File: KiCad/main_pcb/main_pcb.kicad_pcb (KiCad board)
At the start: 0 parts

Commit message: feat(KiCad): Continues work
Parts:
- added C1: 100nF, Capacitor_SMD:C_0201_0603Metric_Pad0.64x0.40mm_HandSolder, F.Cu at (194.6, 71.0)
- added C2: 100nF, Capacitor_SMD:C_0201_0603Metric_Pad0.64x0.40mm_HandSolder, F.Cu at (179.9, 77.0)
- added C20: 10uF, Capacitor_SMD:C_0201_0603Metric_Pad0.64x0.40mm_HandSolder, F.Cu at (183.1, 89.0)
- added C21: 100nF, Capacitor_SMD:C_0201_0603Metric_Pad0.64x0.40mm_HandSolder, F.Cu at (192.6, 85.5)
- added C22: 100nF, Capacitor_SMD:C_0201_0603Metric_Pad0.64x0.40mm_HandSolder, F.Cu at (168.0, 94.0)
- added C23: 100nF, Capacitor_SMD:C_0201_0603Metric_Pad0.64x0.40mm_HandSolder, F.Cu at (185.9, 92.5)
- added C24: 100nF, Capacitor_SMD:C_0201_0603Metric_Pad0.64x0.40mm_HandSolder, F.Cu at (175.1, 95.0)
- added C25: 100nF, Capacitor_SMD:C_0201_0603Metric_Pad0.64x0.40mm_HandSolder, F.Cu at (188.6, 100.0)
- added C26: 100nF, Capacitor_SMD:C_0201_0603Metric_Pad0.64x0.40mm_HandSolder, F.Cu at (179.1, 98.0)
- added C27: 100nF, Capacitor_SMD:C_0201_0603Metric_Pad0.64x0.40mm_HandSolder, F.Cu at (183.1, 103.0)
- added C28: 100nF, Capacitor_SMD:C_0201_0603Metric_Pad0.64x0.40mm_HandSolder, F.Cu at (172.6, 89.0)
- added C29: 100nF, Capacitor_SMD:C_0201_0603Metric_Pad0.64x0.40mm_HandSolder, F.Cu at (190.6, 96.0)
- added C3: 27pF, Capacitor_SMD:C_0201_0603Metric_Pad0.64x0.40mm_HandSolder, F.Cu at (184.0, 74.5)
- added C30: 100nF, Capacitor_SMD:C_0201_0603Metric_Pad0.64x0.40mm_HandSolder, F.Cu at (166.5, 99.0)
- added C31: 100nF, Capacitor_SMD:C_0201_0603Metric_Pad0.64x0.40mm_HandSolder, F.Cu at (177.1, 104.0)
- added C32: 100nF, Capacitor_SMD:C_0201_0603Metric_Pad0.64x0.40mm_HandSolder, F.Cu at (196.6, 99.0)
- added C33: 100nF, Capacitor_SMD:C_0201_0603Metric_Pad0.64x0.40mm_HandSolder, F.Cu at (192.5, 106.5)
- added C4: 27pF, Capacitor_SMD:C_0201_0603Metric_Pad0.64x0.40mm_HandSolder, F.Cu at (186.9, 78.0)
- added C5: 100nF, Capacitor_SMD:C_0201_0603Metric_Pad0.64x0.40mm_HandSolder, F.Cu at (187.1, 86.0)
- added C6: 100nF, Capacitor_SMD:C_0201_0603Metric_Pad0.64x0.40mm_HandSolder, F.Cu at (176.6, 67.5)
- added C7: 100nF, Capacitor_SMD:C_0201_0603Metric_Pad0.64x0.40mm_HandSolder, F.Cu at (181.1, 81.8)
- added C8: 0.1uF, Capacitor_SMD:C_0201_0603Metric_Pad0.64x0.40mm_HandSolder, F.Cu at (178.4, 88.0)
- added C9: 0.1uF, Capacitor_SMD:C_0201_0603Metric_Pad0.64x0.40mm_HandSolder, F.Cu at (166.6, 89.0)
- added D1: ~, LED_SMD:LED_0603_1608Metric_Pad1.05x0.95mm_HandSolder, F.Cu at (125.9, 79.2)
- added D2: ~, LED_SMD:LED_0603_1608Metric_Pad1.05x0.95mm_HandSolder, F.Cu at (125.9, 81.0)
- added D3: ~, LED_SMD:LED_0603_1608Metric_Pad1.05x0.95mm_HandSolder, F.Cu at (125.9, 82.8)
- added D4: ~, LED_SMD:LED_0603_1608Metric_Pad1.05x0.95mm_HandSolder, F.Cu at (125.9, 77.5)
- added R1: 10kΩ, Resistor_SMD:R_0201_0603Metric_Pad0.64x0.40mm_HandSolder, F.Cu at (190.1, 89.5)
- added R10: 10kΩ, Resistor_SMD:R_0201_0603Metric_Pad0.64x0.40mm_HandSolder, F.Cu at (170.6, 102.5)
- added R11: 10kΩ, Resistor_SMD:R_0201_0603Metric_Pad0.64x0.40mm_HandSolder, F.Cu at (199.1, 93.5)
- added R2: 5.1kΩ, Resistor_SMD:R_0201_0603Metric_Pad0.64x0.40mm_HandSolder, F.Cu at (180.0, 92.0)
- added R3: 5.1kΩ, Resistor_SMD:R_0201_0603Metric_Pad0.64x0.40mm_HandSolder, F.Cu at (175.1, 85.0)
- added R4: 10kΩ, Resistor_SMD:R_0201_0603Metric_Pad0.64x0.40mm_HandSolder, F.Cu at (133.4, 79.0)
- added R5: 10kΩ, Resistor_SMD:R_0201_0603Metric_Pad0.64x0.40mm_HandSolder, F.Cu at (133.4, 81.2)
- added R6: 10kΩ, Resistor_SMD:R_0201_0603Metric_Pad0.64x0.40mm_HandSolder, F.Cu at (133.4, 83.8)
- added R7: 10kΩ, Resistor_SMD:R_0201_0603Metric_Pad0.64x0.40mm_HandSolder, F.Cu at (133.4, 76.8)
- added R8: 10kΩ, Resistor_SMD:R_0201_0603Metric_Pad0.64x0.40mm_HandSolder, F.Cu at (171.1, 107.0)
- added R9: 10kΩ, Resistor_SMD:R_0201_0603Metric_Pad0.64x0.40mm_HandSolder, F.Cu at (193.6, 92.0)
- added U1: ~, Package_QFP:TQFP-100_14x14mm_P0.5mm, F.Cu at (155.3, 76.5)
- added U8: CH340C, lilys_pad:CH340C, F.Cu at (146.9, 88.4)
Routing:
- net /SS: track 0.00 -> 15.0 mm
- net /MISO: track 0.00 -> 15.0 mm
- net /SCK: track 0.00 -> 14.2 mm
- net /MOSI: track 0.00 -> 14.1 mm
- net Net-(D3-Pad1): track 0.00 -> 6.69 mm
- net Net-(D4-Pad1): track 0.00 -> 6.56 mm
- net Net-(D2-Pad1): track 0.00 -> 6.38 mm
- net Net-(D1-Pad1): track 0.00 -> 6.38 mm
- net GND: track 0.00 -> 5.32 mm, vias 0 -> 5
- added copper zone on B.Cu, net GND
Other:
- copper layers 0 -> 2

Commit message: feat(KiCad): Continues work
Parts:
- added J3: ~, Connector_JST:JST_XH_B10B-XH-A_1x10_P2.50mm_Vertical, F.Cu at (110.5, 57.9)
- added J4: 2X4 Header, Connector_JST:JST_XH_B8B-XH-A_1x08_P2.50mm_Vertical, F.Cu at (110.5, 65.7)
- added J5: 1x1 Header, Connector_JST:JST_XH_B1B-XH-AM_1x01_P2.50mm_Vertical, F.Cu at (110.5, 81.2)
- added J6: 1x1 Header, Connector_JST:JST_XH_B1B-XH-AM_1x01_P2.50mm_Vertical, F.Cu at (125.5, 95.0)
- added S2: ~, Button_Switch_THT:SW_PUSH-12mm, F.Cu at (138.5, 102.5)
- added Y1: ~, Crystal:Crystal_SMD_ECS_CSM3X-2Pin_7.6x4.1mm, F.Cu at (158.5, 94.2)
- moved R1 37.8 mm to (154.5, 102.4), turned to -90 degrees
- moved C4 37.8 mm to (152.8, 94.2)
- moved C3 28.0 mm to (164.2, 94.2), turned to 180 degrees
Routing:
- net uC_Reset: track 0.00 -> 22.1 mm
- net Net-(U1-XTAL1): track 0.00 -> 16.0 mm
- net Net-(U1-XTAL2): track 0.00 -> 10.3 mm
- net Net-(C4-Pad2): track 0.00 -> 2.53 mm
- net Net-(C3-Pad2): track 0.00 -> 2.51 mm

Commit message: feat(KiCad): Continues work
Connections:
- net Net-(U1-XTAL1) renamed /Y-
- net Net-(U1-XTAL2) renamed /Y+
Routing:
- net /Y-: track 16.0 -> 0.00 mm
- net /Y+: track 10.3 -> 0.00 mm
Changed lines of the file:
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@@
 	(net 44 "unconnected-(U1-PG5-Pad1)")
 	(net 45 "unconnected-(U1-PE0-Pad2)")
-	(net 46 "Net-(U1-XTAL2)")
+	(net 46 "/Y-")
 	(net 47 "/C4")
 	(net 48 "unconnected-(U1-PE3-Pad5)")
@@
 	(net 85 "/C5")
 	(net 86 "/C2")
-	(net 87 "Net-(U1-XTAL1)")
+	(net 87 "/Y+")
 	(net 88 "unconnected-(U1-PD5-Pad48)")
 	(net 89 "unconnected-(U1-PD4-Pad47)")
@@
 			(layers "F.Cu" "F.Mask" "F.Paste")
 			(roundrect_rratio 0.25)
-			(net 46 "Net-(U1-XTAL2)")
+			(net 87 "/Y+")
 			(pinfunction "XTAL2")
 			(pintype "output")
@@
 			(layers "F.Cu" "F.Mask" "F.Paste")
 			(roundrect_rratio 0.25)
-			(net 87 "Net-(U1-XTAL1)")
+			(net 46 "/Y-")
 			(pinfunction "XTAL1")
 			(pintype "input")
@@
 			(layers "F.Cu" "F.Mask")
 			(roundrect_rratio 0.25)
-			(net 87 "Net-(U1-XTAL1)")
+			(net 46 "/Y-")
 			(pintype "passive")
 		)
@@
 			(layers "F.Cu" "F.Mask")
 			(roundrect_rratio 0.25)
-			(net 46 "Net-(U1-XTAL2)")
+			(net 87 "/Y+")
 			(pintype "passive")
 		)
@@
 	)
 	(segment
-		(start 152.8375 93.751544)
-		(end 152.41 94.179044)
-		(width 0.2)
-		(layer "F.Cu")
-		(net 46)
-	)
-	(segment
-		(start 152.41 94.179044)
-		(end 152.41 94.25)
-		(width 0.2)
-		(layer "F.Cu")
-		(net 46)
-	)
-	(segment
-		(start 152.8375 84.1625)
-		(end 152.8375 93.751544)
-		(width 0.2)
-		(layer "F.Cu")
-		(net 46)
-	)
-	(segment
 		(start 134.59 80.5)
 		(end 147.675 80.5)
@@
 	)
 	(segment
-		(start 163.874999 93.35)
-		(end 164.575 94.050001)
-		(width 0.2)
-		(layer "F.Cu")
-		(net 87)
-	)
-	(segment
-		(start 164.575 94.050001)
-		(end 164.575 94.25)
-		(width 0.2)
-		(layer "F.Cu")
-		(net 87)
-	)
-	(segment
-		(start 161.75509 93.35)
-		(end 163.874999 93.35)
-		(width 0.2)
-		(layer "F.Cu")
-		(net 87)
-	)
-	(segment
-		(start 153.3375 84.93241)
-		(end 161.75509 93.35)
-		(width 0.2)
-		(layer "F.Cu")
-		(net 87)
-	)
-	(segment
-		(start 153.3375 84.1625)
-		(end 153.3375 84.93241)
-		(width 0.2)
-		(layer "F.Cu")
-		(net 87)
-	)
-	(segment

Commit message: feat(KiCad): Continues work
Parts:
- removed C21, C22, C23, C24, C25, C26, C27, C28, C29, C30, C31, C32, C33: 100nF, Capacitor_SMD:C_0201_0603Metric_Pad0.64x0.40mm_HandSolder
- removed S2: ~, Button_Switch_THT:SW_PUSH-12mm
- removed U8: CH340C, lilys_pad:CH340C
- added C10: 0.1uF, Capacitor_SMD:C_0201_0603Metric_Pad0.64x0.40mm_HandSolder, F.Cu at (165.5, 64.4)
- added C11: 0.1uF, Capacitor_SMD:C_0201_0603Metric_Pad0.64x0.40mm_HandSolder, F.Cu at (167.5, 64.4)
- added C12: 100nF, Capacitor_SMD:C_0201_0603Metric_Pad0.64x0.40mm_HandSolder, F.Cu at (143.4, 96.5)
- added C13: 100nF, Capacitor_SMD:C_0201_0603Metric_Pad0.64x0.40mm_HandSolder, F.Cu at (143.4, 98.2)
- added C14: 100nF, Capacitor_SMD:C_0201_0603Metric_Pad0.64x0.40mm_HandSolder, F.Cu at (143.4, 100.0)
- added C15: 100nF, Capacitor_SMD:C_0201_0603Metric_Pad0.64x0.40mm_HandSolder, F.Cu at (143.4, 101.8)
- added C16: 100nF, Capacitor_SMD:C_0201_0603Metric_Pad0.64x0.40mm_HandSolder, F.Cu at (143.4, 103.5)
- added C17: 100nF, Capacitor_SMD:C_0201_0603Metric_Pad0.64x0.40mm_HandSolder, F.Cu at (146.3, 96.5)
- added C18: 100nF, Capacitor_SMD:C_0201_0603Metric_Pad0.64x0.40mm_HandSolder, F.Cu at (146.3, 98.2)
- added C19: 100nF, Capacitor_SMD:C_0201_0603Metric_Pad0.64x0.40mm_HandSolder, F.Cu at (146.3, 100.0)
- added J2: ~, Connector_JST:JST_XH_B10B-XH-A_1x10_P2.50mm_Vertical, F.Cu at (108.5, 83.0)
- added S1: ~, Button_Switch_THT:SW_PUSH-12mm, F.Cu at (125.4, 92.7)
- added U2: CH340C, Lilibrary:SOIC127P600X180-16N, F.Cu at (167.0, 74.5)
- added U3: JSMSEMI AMS1117-3.3V, Lilibrary:SOT229P700X180-4N, F.Cu at (167.2, 57.2)
- added U4: TI TXB0104DR, Lilibrary:SOIC127P600X175-14N, F.Cu at (166.1, 141.7)
- added U6: TI TXB0104DR, Lilibrary:SOIC127P600X175-14N, F.Cu at (175.0, 141.7)
- added U9: TI TXB0104DR, Lilibrary:SOIC127P600X175-14N, F.Cu at (184.0, 141.7)
- C2: value 100nF -> 27pF
- C20: value 10uF -> 100nF
- C4: value 27pF -> 100nF
- C8: value 0.1uF -> 100nF
- C9: value 0.1uF -> 10uF
- J3: value ~ -> 1x6 Header; footprint Connector_JST:JST_XH_B10B-XH-A_1x10_P2.50mm_Vertical -> Lilibrary:1x6 Header
- J4: value 2X4 Header -> 1x1 Header; footprint Connector_JST:JST_XH_B8B-XH-A_1x08_P2.50mm_Vertical -> Lilibrary:1x1 Header
- J5: footprint Connector_JST:JST_XH_B1B-XH-AM_1x01_P2.50mm_Vertical -> Lilibrary:1x1 Header
- J6: value 1x1 Header -> USB-C; footprint Connector_JST:JST_XH_B1B-XH-AM_1x01_P2.50mm_Vertical -> Lilibrary:HRO_TYPE-C-31-M-12
- R2, R3: value 5.1kΩ -> 330Ω
- R4, R5: value 10kΩ -> 330Ω
- R6, R7: value 10kΩ -> 5.1kΩ
- moved J3 103.9 mm to (132.5, 159.5), turned to -90 degrees
- moved C1 75.7 mm to (129.3, 109.5), turned to 0 degrees
- moved U1 70.8 mm to (132.5, 143.5), turned to 90 degrees
- moved C5 65.3 mm to (129.3, 116.5)
- moved J6 61.3 mm to (180.5, 122.0)
- moved C2 61.1 mm to (129.3, 111.2)
- moved R2 51.0 mm to (132.1, 109.5)
- moved R11 50.4 mm to (149.1, 100.0)
- moved R3 50.3 mm to (132.1, 111.2)
- moved J5 44.8 mm to (155.3, 83.0)
- moved R9 44.7 mm to (149.1, 96.5)
- moved J4 41.6 mm to (148.3, 83.0)
- moved D4 41.4 mm to (135.8, 117.7), turned to 0 degrees
- moved C3 39.6 mm to (129.3, 113.0), turned to 0 degrees
- moved C20 39.0 mm to (146.3, 101.8)
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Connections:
- C1 pad 1: GND -> VCC
- C1 pad 2: Net-(U8-V3) -> VCC
- C2 pad 1: Net-(U8-DTR#) -> /Y-
- C2 pad 2: uC_Reset -> Net-(C2-Pad2)
- C20 pad 1: VCC -> GND
- C20 pad 2: GND -> 3V3
- C3 pad 1: /Y- -> /Y+
- C4 pad 1: /Y+ -> Net-(U1-AREF)
- C4 pad 2: Net-(C4-Pad2) -> GND
- C5 pad 1: VCC -> GND
- C5 pad 2: VCC -> GND
- C6 pad 1: GND -> VCC
- C7 pad 2: VCC -> uC_Reset
- C8 pad 1: VCC -> GND
- C8 pad 2: GND -> Net-(U2-V3)
- J3 pad 1: /TCK -> /SS
- J3 pad 2: GND -> /MISO
- J3 pad 3: /TDO -> /MOSI
- J3 pad 4: VCC -> /SCK
- J3 pad 5: /TMS -> VCC
- J3 pad 6: uC_Reset -> GND
- J4 pad 1: /SCK -> VCC
- R2 pad 1: Net-(J2-CC1) -> Net-(D1-Pad1)
- R2 pad 2: GND -> /SS
- R3 pad 1: Net-(J2-CC2) -> Net-(D2-Pad1)
- R3 pad 2: GND -> /MISO
- R4 pad 1: Net-(D1-Pad1) -> Net-(D3-Pad1)
- R4 pad 2: /SCK -> /MOSI
- R5 pad 1: Net-(D2-Pad1) -> Net-(D4-Pad1)
- R5 pad 2: /MOSI -> /SCK
- R6 pad 1: Net-(D3-Pad1) -> Net-(J6-CC1)
- R6 pad 2: /MISO -> GND
- R7 pad 1: Net-(D4-Pad1) -> Net-(J6-CC2)
- R7 pad 2: /SS -> GND
- U1 pad 12: unconnected-(U1-PH0-Pad12) -> /screens/LED/BL
- Y1 pad 1: Net-(C3-Pad2) -> Net-(C2-Pad2)
- Y1 pad 2: Net-(C4-Pad2) -> Net-(C3-Pad2)
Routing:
- net uC_Reset: track 22.1 -> 0.00 mm
- net /SS: track 15.0 -> 0.00 mm
- net /MISO: track 15.0 -> 0.00 mm
- net /SCK: track 14.2 -> 0.00 mm
- net /MOSI: track 14.1 -> 0.00 mm
- net VCC: track 0.00 -> 11.4 mm
- net Net-(D3-Pad1): track 6.69 -> 0.00 mm
- net Net-(D4-Pad1): track 6.56 -> 0.00 mm
- net Net-(D2-Pad1): track 6.38 -> 0.00 mm
- net Net-(D1-Pad1): track 6.38 -> 0.00 mm
- net GND: track 5.32 -> 0.00 mm, vias 5 -> 0
- net Net-(C4-Pad2): track 2.53 -> 0.00 mm
- net Net-(C3-Pad2): track 2.51 -> 0.00 mm
- removed copper zone on B.Cu, net GND

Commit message: Adds Main PCB layout (#38)
* feat(PCB): PCB first draft
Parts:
- removed C5: 100nF, Capacitor_SMD:C_0201_0603Metric_Pad0.64x0.40mm_HandSolder
- removed J2: ~, Connector_JST:JST_XH_B10B-XH-A_1x10_P2.50mm_Vertical
- removed R10, R11, R8, R9: 10kΩ, Resistor_SMD:R_0201_0603Metric_Pad0.64x0.40mm_HandSolder
- added J1: 1x21 Header, Lilibrary:1x21 Header, F.Cu at (122.0, 173.0)
- added J7: 1X7 Header, Lilibrary:1x7 Header, F.Cu at (140.4, 64.7)
- added J8: 1X7 Header, Lilibrary:1x7 Header, F.Cu at (121.5, 64.7)
- added J9: 1x13 Header, Lilibrary:1x13 Header, F.Cu at (94.8, 64.8)
- C1, C10, C11, C12, C13, C14, C15, C16, C17, C18, C19, C2, C20, C3, C4, C6, C7, C8, C9: footprint Capacitor_SMD:C_0201_0603Metric_Pad0.64x0.40mm_HandSolder -> Capacitor_SMD:C_0603_1608Metric_Pad1.08x0.95mm_HandSolder
- J6: value USB-C -> TYPE-C-31-M-12
- R1, R2, R3, R4, R5, R6, R7: footprint Resistor_SMD:R_0201_0603Metric_Pad0.64x0.40mm_HandSolder -> Resistor_SMD:R_0603_1608Metric_Pad0.98x0.95mm_HandSolder
- U1: value ~ -> ATmega 2560
- Y1: footprint Crystal:Crystal_SMD_ECS_CSM3X-2Pin_7.6x4.1mm -> Crystal:Crystal_SMD_0603-4Pin_6.0x3.5mm_HandSoldering
- moved U4 131.9 mm to (67.8, 53.7), turned to -90 degrees
- moved U6 91.0 mm to (107.6, 80.6), turned to 90 degrees
- moved C12 86.9 mm to (71.6, 47.6), turned to -90 degrees
- moved C13 82.8 mm to (70.9, 58.4)
- moved U9 82.2 mm to (132.9, 77.3), turned to 90 degrees
- moved C14 71.1 mm to (80.4, 67.2)
- moved U3 69.3 mm to (163.1, 126.3), turned to 90 degrees
- moved C6 67.6 mm to (163.7, 145.0), turned to -90 degrees
- moved U2 65.6 mm to (159.3, 139.7), turned to -90 degrees
- moved C7 65.1 mm to (159.9, 145.2), turned to -90 degrees
- moved J3 65.0 mm to (120.3, 95.6), turned to 90 degrees
- moved C8 52.9 mm to (160.0, 134.2), turned to -90 degrees
- moved C10 52.1 mm to (169.2, 116.3), turned to 90 degrees
- moved C11 52.0 mm to (171.0, 116.3), turned to 90 degrees
- moved C9 51.8 mm to (167.5, 116.3), turned to 90 degrees
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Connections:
- J6 pad A1_B12: (no net) -> GND
- J6 pad A4_B9: (no net) -> VCC
- J6 pad B1_A12: (no net) -> GND
- J6 pad B4_A9: (no net) -> VCC
- J6 pad S1: (no net) -> GND
- J6 pad S2: (no net) -> GND
- J6 pad S3: (no net) -> GND
- J6 pad S4: (no net) -> GND
- U1 pad 90: /TDI -> unconnected-(U1-PF7-Pad90)
- U1 pad 91: /TDO -> unconnected-(U1-PF6-Pad91)
- U1 pad 92: /TMS -> unconnected-(U1-PF5-Pad92)
- U1 pad 93: /TCK -> unconnected-(U1-PF4-Pad93)
- U6 pad 13: Net-(U6-B1) -> /screens/CS Main Screen 3V3
- U9 pad 3: /screens/CS Right Eye -> /screens/RST Eyes
- U9 pad 4: /screens/RST Eyes -> /screens/CS Right Eye
- Y1 pad 1: Net-(C2-Pad2) -> Net-(C3-Pad2)
- Y1 pad 2: Net-(C3-Pad2) -> GND
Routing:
- net VCC: track 11.4 -> 360.1 mm, vias 0 -> 7
- net 3V3: track 0.00 -> 217.7 mm, vias 0 -> 2
- net /MOSI: track 0.00 -> 204.1 mm, vias 0 -> 8
- net /SCK: track 0.00 -> 202.3 mm, vias 0 -> 8
- net /D/C: track 0.00 -> 198.4 mm, vias 0 -> 4
- net uC_Reset: track 0.00 -> 191.8 mm
- net /MISO: track 0.00 -> 171.0 mm, vias 0 -> 5
- net /R3: track 0.00 -> 94.3 mm
- net /R2: track 0.00 -> 82.7 mm
- net /R1: track 0.00 -> 61.3 mm
- net /SCL: track 0.00 -> 58.7 mm
- net /Power and UART/UART_TX: track 0.00 -> 58.0 mm, vias 0 -> 2
- net /SDA: track 0.00 -> 57.2 mm
- net /Power and UART/UART_RX: track 0.00 -> 56.3 mm, vias 0 -> 2
- net /R4: track 0.00 -> 56.1 mm, vias 0 -> 2
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- added copper zone on B.Cu, net GND
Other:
- board outline added: 119.9 x 132 mm

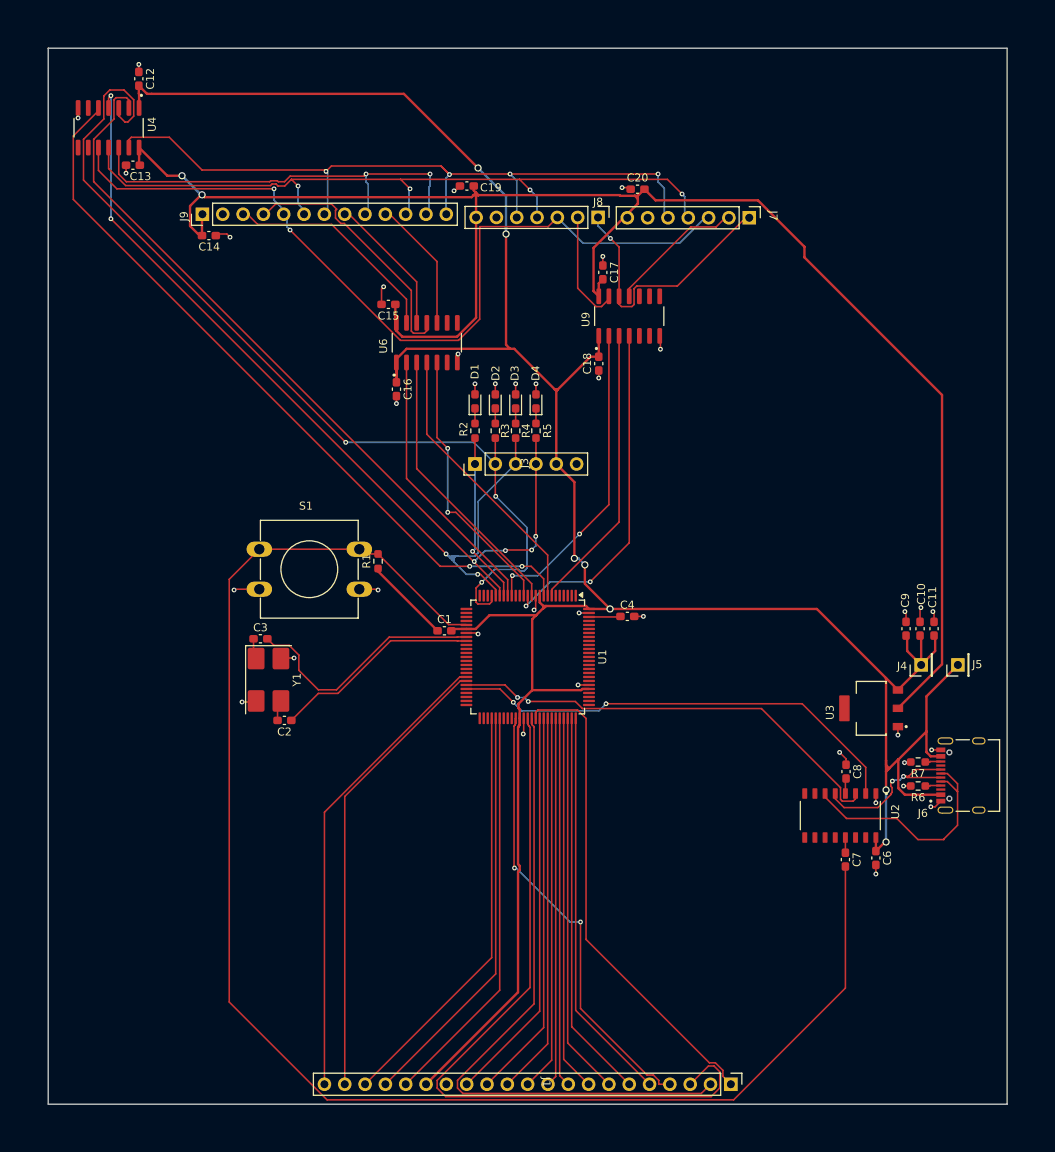
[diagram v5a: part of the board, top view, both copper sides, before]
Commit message: feat(PCB Layout): Refactors Main PCB layout to achieve smaller form factor and adds JLCPCB constraints.
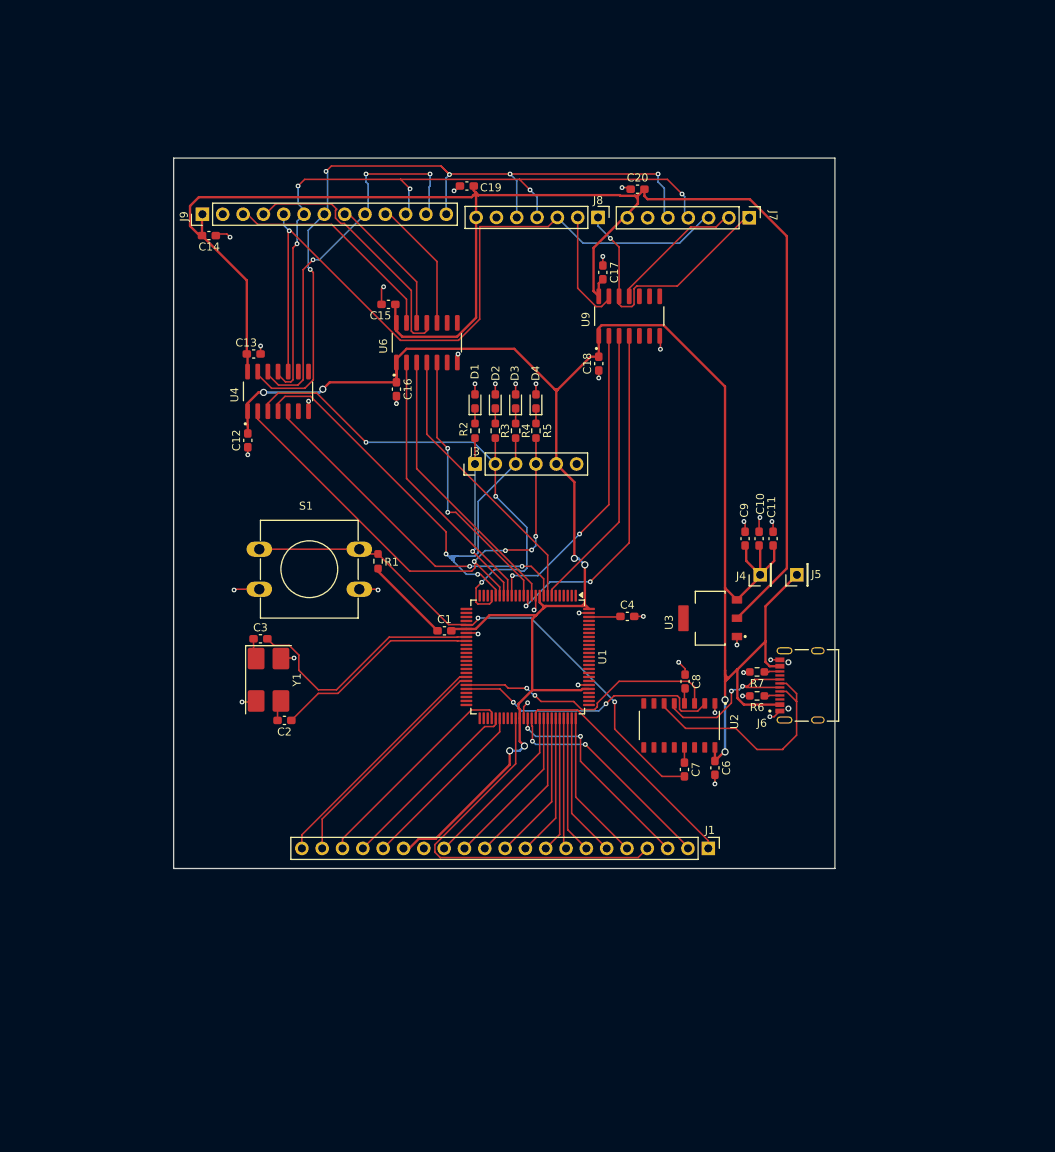
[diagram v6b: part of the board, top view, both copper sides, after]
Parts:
- moved C12 47.2 mm to (85.2, 92.8), turned to 90 degrees
- moved U4 39.2 mm to (89.0, 86.7), turned to 90 degrees
- moved J1 29.6 mm to (119.2, 143.5)
- moved C13 28.0 mm to (86.0, 82.0), turned to 180 degrees
- moved C10 23.1 mm to (149.1, 105.1)
- moved C11 23.1 mm to (150.9, 105.1)
- moved C9 23.1 mm to (147.4, 105.1)
- moved J6 23.1 mm to (156.5, 123.4)
- moved R6 23.1 mm to (148.9, 124.7)
- moved R7 23.1 mm to (148.9, 121.7)
- moved U3 23.1 mm to (143.0, 115.0)
- moved C8 23.1 mm to (139.9, 122.9)
- moved J4 23.1 mm to (149.5, 109.3)
- moved J5 23.1 mm to (154.1, 109.3)
- moved U2 23.1 mm to (139.2, 128.4)
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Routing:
- net uC_Reset: track 191.8 -> 66.8 mm, vias 0 -> 2
- net VCC: track 360.1 -> 287.5 mm, vias 7 -> 8
- net /R3: track 94.3 -> 26.8 mm, vias 0 -> 2
- net /D/C: track 198.4 -> 136.7 mm, vias 4 -> 3
- net /MISO: track 171.0 -> 111.3 mm, vias 5 -> 6
- net /R2: track 82.7 -> 27.8 mm, vias 0 -> 2
- net /MOSI: track 204.1 -> 155.0 mm, vias 8 -> 7
- net /SCK: track 202.3 -> 159.5 mm, vias 8 -> 9
- net /R1: track 61.3 -> 30.2 mm
- net /C4: track 47.0 -> 16.0 mm
- net /C3: track 47.9 -> 17.2 mm
- net /C1: track 49.6 -> 18.9 mm
- net /C2: track 48.7 -> 18.1 mm
- net /C5: track 46.2 -> 17.0 mm
- net /SLD_SW3: track 50.6 -> 22.3 mm
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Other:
- board size 119.9 x 132 mm -> 82.7 x 88.8 mm
